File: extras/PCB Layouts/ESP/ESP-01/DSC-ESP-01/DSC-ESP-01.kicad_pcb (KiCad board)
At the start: 2 copper layers, 32 x 12.7 mm, 9 parts, among them J1 Conn_01x04_Pin, J2 Conn_01x02_Pin, Q1 2N7000, Q2 2N7000, Q3 2N7000, Q4 2N7000, U1 ESP-01

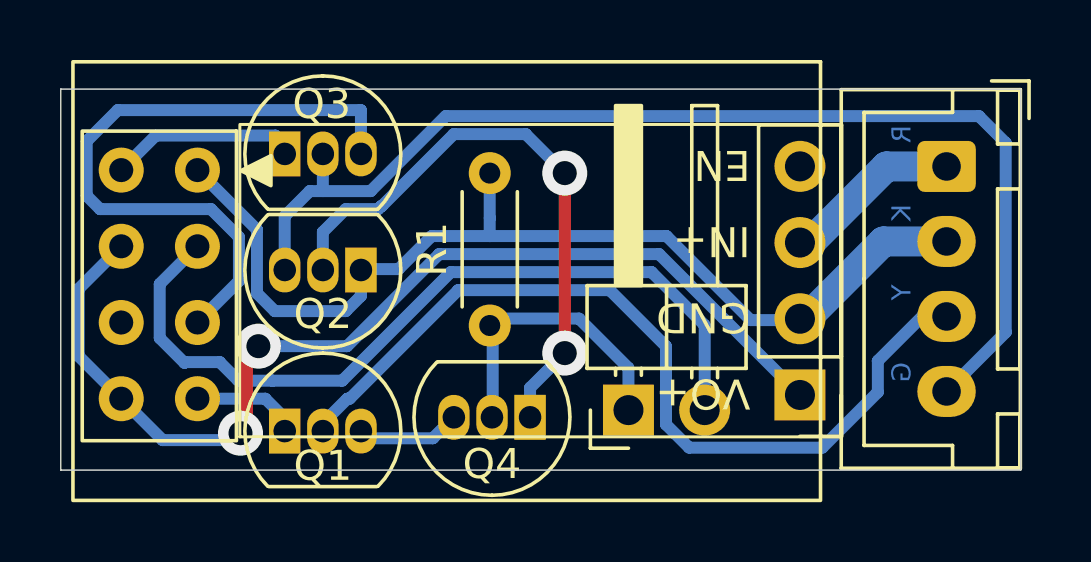
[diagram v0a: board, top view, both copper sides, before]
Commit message: Moved traces to allow milling with a wider (or dull) bit. Changed ESP-01 landing holes to 1.0mm, and standardized other holes.
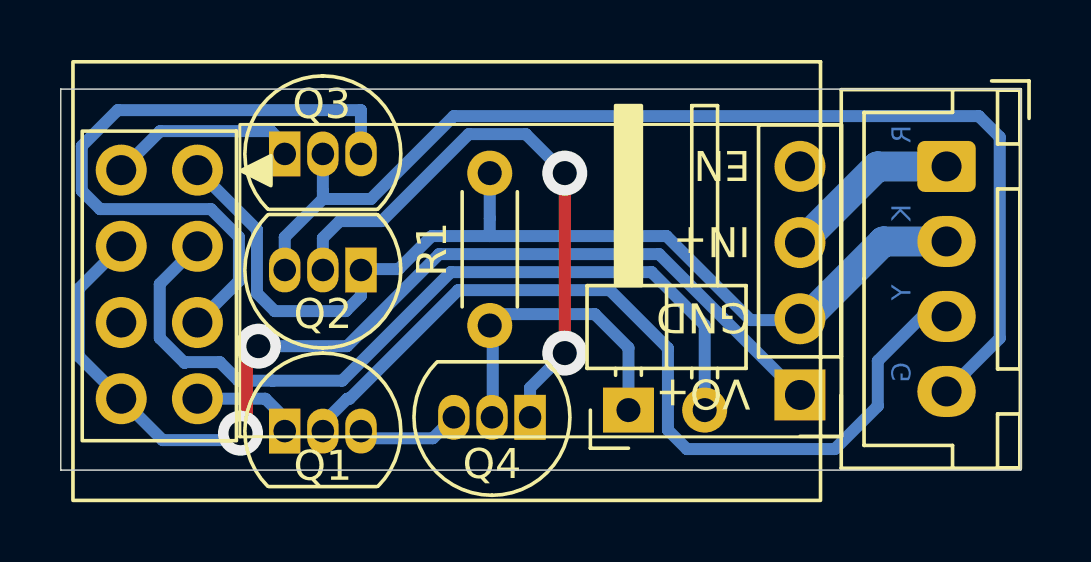
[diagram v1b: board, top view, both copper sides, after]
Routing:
- net /VCC: track 35.8 -> 35.2 mm
- net Net-(J2-Pin_1): track 10.5 -> 11.0 mm

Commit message: Redesigned DSC-ESP-01.kicad_pcb to use the `TO-92_HandSolder` footprint.
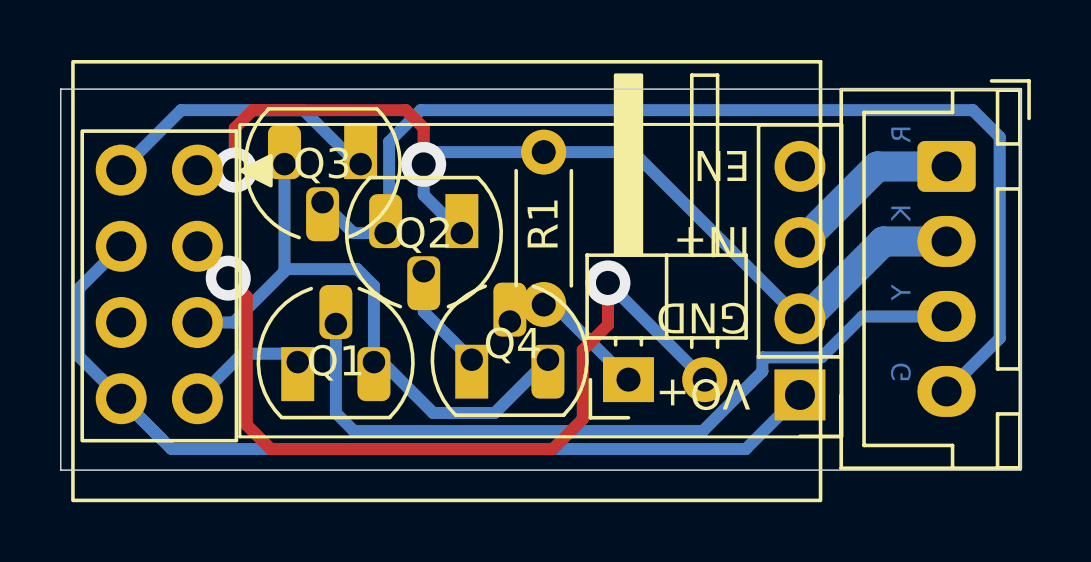
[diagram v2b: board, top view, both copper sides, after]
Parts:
- Q1, Q2, Q3, Q4: footprint Package_TO_SOT_THT:TO-92_Inline -> Package_TO_SOT_THT:TO-92_HandSolder
- moved Q2 3.58 mm to (192.6, 77.0)
- moved Q4 2.73 mm to (192.9, 81.2), turned to 0 degrees
- moved Q3 2.55 mm to (189.2, 74.7), turned to 180 degrees
- moved Q1 2.34 mm to (187.1, 81.3)
- moved R1 1.93 mm to (195.3, 79.4)
- moved J2 1.02 mm to (198.1, 81.9)
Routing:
- net Net-(Q2-G): track 19.9 -> 3.61 mm, vias 2 -> 0
- net Net-(J2-Pin_1): track 11.0 -> 5.02 mm
- net Net-(Q1-D): track 25.1 -> 19.9 mm
- net /Yellow: track 29.4 -> 25.7 mm
- net Net-(Q3-S): track 6.48 -> 9.60 mm
- net /VCC: track 35.2 -> 32.3 mm, vias 2 -> 0
- net /Green: track 37.9 -> 36.0 mm
- net Net-(J2-Pin_2): track 27.9 -> 26.5 mm, vias 0 -> 2
- net /Black: track 34.3 -> 33.3 mm, vias 0 -> 2
